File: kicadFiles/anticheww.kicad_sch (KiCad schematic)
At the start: 423 parts, among them J1 TYPE-C-31-M12_13, J2 ARM JTAG, Q1 AO3401A, Q2 DTC123JKAT146, Q3 DTC123JKAT146, SW1 ESC, SW10 9, SW11 0, SW12 MINUS, SW13 PLUS, SW14 LBKSP, SW15 RBKSP, SW16 Rotary_Encoder_Switch_Chassis, SW17 2U_BKSP, SW18 Rotary_Encoder_Switch_Chassis, SW19 TAB, SW2 1, SW20 Q, SW21 W, SW22 E, SW23 R, SW24 T, SW25 Y, SW26 U, SW27 I, SW28 O, SW29 P, SW3 2, SW30 LBRKT, SW31 RBRKT, SW32 BKSLSH, SW33 PGDN, SW34 ISO_ENTER, SW35 Rotary_Encoder_Switch_Chassis, SW36 CAPS, SW37 A, SW38 S, SW39 D, SW4 3, SW40 F, SW41 G, SW42 H, SW43 J, SW44 K, SW45 L, SW46 COLON, SW47 QUOTE, SW48 ENTER, SW49 HOME, SW5 4, SW50 PGUP, SW51 STEPPED_CAPS, SW52 ISO_TILDE, SW53 Rotary_Encoder_Switch_Chassis, SW54 LSHFT, SW55 ISO_BKLSH, SW56 Z, SW57 X, SW58 C, SW59 V, SW6 5, SW60 B, SW61 N, SW62 M, SW63 COMMA, SW64 DOT, SW65 SLSH, SW66 175_RSHFT, SW67 UP, SW68 END, SW69 ISO_LSHFT, SW7 6, SW70 275_RSHFT, SW71 LCTRL, SW72 LGUI, SW73 LALT, SW74 SPC, SW75 RALT, SW76 RGUI, SW77 RCTRL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

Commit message: Finish routing, DRC pending
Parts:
- removed R26: 10k, Resistor_SMD:R_0805_2012Metric, symbol Device:R
- added D89, D90, D91, D92: 1N4148W, acheron_Components:D_SOD-123, symbol Device:D
- renumbered SW16 to ROT1, SW18 to ROT2, SW35 to ROT3, SW53 to ROT4
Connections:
- net ENCB: now also ROT1.B, ROT2.B, ROT3.B, ROT4.B
- net GND: now also ROT1.S (Shield), ROT2.S (Shield), ROT3.S (Shield), ROT4.S (Shield)
- net RGB_3V3: now also U3.28 (SPI2_MOSI/I2S2_SD/PB15)
- net ROTB: now also U3.18 (PB0/TIM3_CH3/ADC_IN8)
- net R0: now reaches D1.1 (K), D10.1 (K), D11.1 (K), D12.1 (K), D13.1 (K), D14.1 (K), D15.1 (K), D2.1 (K), D3.1 (K), D4.1 (K), D5.1 (K), D6.1 (K), D7.1 (K), D8.1 (K), D9.1 (K)
- net R0: now also U3.30 (TIM1_CH2/PA9)
- net ENCA: now reaches ROT2.A
- net ENCA: now also R94.2, R96.1, ROT1.A, ROT3.A, ROT4.A
- net at ROT2.C: now also D90.2 (A)
- net C14: now reaches ROT2.S1
- net C14: now also ROT1.S1, ROT4.S1, SW15.1 (Col), SW17.1 (Col), SW33.1 (Col), SW50.1 (Col), SW68.1 (Col), SW80.1 (Col), U3.39 (SPI1_SCK/I2S1_CK/TIM2_CH2/PB3)
- net R2_S2: now reaches ROT2.S2
- net R2_S2: now also D30.2 (A), SW33.2 (Row)
- net C1: now reaches SW2.1 (Col), SW20.1 (Col), SW37.1 (Col), SW55.1 (Col), SW72.1 (Col), SW82.1 (Col)
- net C1: now also U3.11 (PA1/ADC_IN1)
- net R1: now reaches D16.1 (K), D17.1 (K), D18.1 (K), D19.1 (K), D20.1 (K), D21.1 (K), D22.1 (K), D23.1 (K), D24.1 (K), D25.1 (K), D26.1 (K), D27.1 (K), D28.1 (K), D29.1 (K)
- net R1: now also D45.1 (K), U3.38 (PA15), D89.1 (K); no longer D30.1 (K)
- net C13: now reaches SW14.1 (Col), SW32.1 (Col), SW34.1 (Col), SW49.1 (Col), SW67.1 (Col), SW79.1 (Col)
- net C13: now also ROT3.S1, U3.40 (SPI1_MISO/I2S1_MCK/TIM3_CH1/PB4)
- net R5: now reaches D32.1 (K), D33.1 (K), D34.1 (K), D35.1 (K), D36.1 (K), D37.1 (K), D38.1 (K), D39.1 (K), D40.1 (K), D41.1 (K), D42.1 (K), D43.1 (K), D44.1 (K)
- net R5: now also D30.1 (K), D90.1 (K); no longer D31.1 (K), D45.1 (K)
- net C12: now reaches SW13.1 (Col), SW31.1 (Col), SW48.1 (Col), SW52.1 (Col), SW66.1 (Col), SW70.1 (Col), SW78.1 (Col)
- net C12: now also U3.41 (SPI1_MOSI/I2S1_SD/TIM3_CH2/PB5)
- net C2: now reaches SW21.1 (Col), SW3.1 (Col), SW38.1 (Col), SW56.1 (Col), SW73.1 (Col), SW83.1 (Col)
- net C2: now also U3.10 (PA0/ADC_IN0)
- net C8: now reaches SW27.1 (Col), SW44.1 (Col), SW62.1 (Col), SW87.1 (Col), SW9.1 (Col), SW90.1 (Col)
- net C8: now also U3.46 (SPI2_NSS/I2S2_WS/I2C1_SDA/TIM17_CH1/PB9)
- net C5: now reaches SW24.1 (Col), SW41.1 (Col), SW59.1 (Col), SW6.1 (Col)
- net C5: now also U3.4 (PC15/OSC32_OUT)
- net C11: now reaches SW12.1 (Col), SW30.1 (Col), SW47.1 (Col), SW65.1 (Col), SW77.1 (Col)
- net C11: now also U3.42 (I2C1_SCL/PB6)
- net C6: now reaches SW25.1 (Col), SW42.1 (Col), SW60.1 (Col), SW7.1 (Col), SW74.1 (Col), SW84.2 (Row), SW86.1 (Col), SW89.1 (Col)
- net C6: now also U3.3 (PC14/OSC32_IN)
- net C7: now reaches SW26.1 (Col), SW43.1 (Col), SW61.1 (Col), SW8.1 (Col)
- net C7: now also U3.2 (PC13)
- net ROTA: now reaches C17.1, R96.2
- net ROTA: now also U3.17 (PA7/TIM3_CH2/TIM14_CH1/ADC_IN7)
- net C10: now reaches SW11.1 (Col), SW29.1 (Col), SW46.1 (Col), SW64.1 (Col), SW76.1 (Col)
- net C10: now also U3.43 (2C1_SDA/PB7)
- net R4: now reaches D61.1 (K), D62.1 (K), D63.1 (K), D64.1 (K), D65.1 (K), D66.1 (K), D67.1 (K), D68.1 (K), D69.1 (K), D70.1 (K), D71.1 (K), D72.1 (K)
- net R4: now also U3.29 (TIM1_CH1/PA8), D92.1 (K)
- net C0: now reaches SW1.1 (Col), SW19.1 (Col), SW36.1 (Col), SW51.1 (Col), SW54.1 (Col), SW69.1 (Col), SW71.1 (Col), SW81.1 (Col)
- net R3_S2: now reaches D44.2 (A), SW49.2 (Row)
- net R3_S2: now also ROT3.S2
- net R3: now reaches D46.1 (K), D47.1 (K), D48.1 (K), D49.1 (K), D50.1 (K), D51.1 (K), D52.1 (K), D53.1 (K), D54.1 (K), D55.1 (K), D56.1 (K), D57.1 (K), D58.1 (K), D59.1 (K), D60.1 (K)
- net R3: now also U3.27 (SPI2_MISO/I2S2_MCK/I2C2_SDA/TIM15_CH1/PB14), D91.1 (K)
- net C4: now reaches SW23.1 (Col), SW40.1 (Col), SW5.1 (Col), SW58.1 (Col), SW85.1 (Col), SW88.1 (Col)
- net C4: now also U3.5 (PF0/OSC_IN)
- net R2: now reaches U3.31 (TIM1_CH3/PA10)
- net R2: now also D31.1 (K)
- net C9: now reaches U3.45 (I2C1_SCL/TIM16_CH1/PB8)
- net C9: now also SW10.1 (Col), SW28.1 (Col), SW45.1 (Col), SW63.1 (Col), SW75.1 (Col)
- net C3: now reaches U3.6 (PF1/OSC_OUT)
- net C3: now also SW22.1 (Col), SW39.1 (Col), SW4.1 (Col), SW57.1 (Col)
- net at ROT3.C: now also D91.2 (A)
- net R4_S2: now reaches D60.2 (A), SW68.2 (Row)
- net R4_S2: now also ROT4.S2
- net R1_S2: now reaches D45.2 (A), SW50.2 (Row)
- net R1_S2: now also ROT1.S2
- net at ROT4.C: now also D92.2 (A)
- net at ROT1.C: now also D89.2 (A)
- no-connect marks 1 -> 2
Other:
- moved on the sheet: D30, D45, SW33, SW50

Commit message: Organize schematic and reset annotations
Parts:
- added SW87: RALT_125, acheron_MX_SolderMask:MX125, symbol acheronSymbols:MXSwitch
- added SW88: RGUI_125, acheron_MX_SolderMask:MX125, symbol acheronSymbols:MXSwitch
- added SW89: RGUI_150, acheron_MX_SolderMask:MX150, symbol acheronSymbols:MXSwitch
- U2: renamed from U3; value STM32F072-LQFP48 -> STM32F072CBT6
- renumbered C17 to C1, C8 to C10, C9 to C11, C10 to C12, C11 to C13, C12 to C14, C13 to C15, C14 to C16, C15 to C17, C16 to C18, C18 to C2, C26 to C23, C27 to C24, C29 to C25, C30 to C26, C23 to C27, C24 to C28, C25 to C29, C1 to C3, C28 to C30, C2 to C4, C3 to C5, C4 to C6, C5 to C7, C6 to C8, C7 to C9, D89 to D1, D78 to D10, D79 to D11, D80 to D12, D81 to D13, D82 to D14, D83 to D15, D84 to D16, D85 to D17, D86 to D18, D1 to D19, D90 to D2, D2 to D20, D3 to D21, D4 to D22, D5 to D23, D6 to D24, D7 to D25, D8 to D26, D9 to D27, D10 to D28, D11 to D29, D91 to D3, D12 to D30, D13 to D31, D14 to D32, D15 to D33, D16 to D34, D17 to D35, D18 to D36, D19 to D37, D20 to D38, D21 to D39, D92 to D4, D22 to D40, D23 to D41, D24 to D42, D25 to D43, D26 to D44, D27 to D45, D28 to D46, D29 to D47, D45 to D48, D31 to D49, D73 to D5, D32 to D50, D33 to D51, D34 to D52, D35 to D53, D36 to D54, D37 to D55, D38 to D56, D39 to D57, D40 to D58, D41 to D59, D74 to D6, D42 to D60, D43 to D61, D44 to D62, D30 to D63, D46 to D64, D47 to D65, D48 to D66, D49 to D67, D50 to D68, D51 to D69, D75 to D7, D52 to D70, D53 to D71, D54 to D72, D55 to D73, D56 to D74, D57 to D75, D58 to D76, D59 to D77, D60 to D78, D61 to D79, D76 to D8, D62 to D80, D63 to D81, D64 to D82, D65 to D83, D66 to D84, D67 to D85, D68 to D86, D69 to D87, D70 to D88, D71 to D89, D77 to D9, D72 to D90, D87 to D91, D88 to D92, J2 to J1, J1 to J2, R94 to R1, R8 to R10, R101 to R100, R102 to R101, R9 to R11, R27 to R12, R28 to R13, R29 to R14, R30 to R15, R31 to R16, R32 to R17, R33 to R18, R1 to R19, R95 to R2, R2 to R20, R10 to R21, R11 to R22, R12 to R23, R13 to R24, R14 to R25, R15 to R26, R16 to R27, R17 to R28, R18 to R29, R96 to R3, R19 to R30, R20 to R31, R21 to R32, R22 to R33, R23 to R34, R24 to R35, R25 to R36, R34 to R37, R35 to R38, R36 to R39, R97 to R4, R37 to R40, R38 to R41, R39 to R42, R40 to R43, R41 to R44, R42 to R45, R43 to R46, R44 to R47, R45 to R48, R46 to R49, R3 to R5, R47 to R50, R48 to R51, R49 to R52, R50 to R53, R51 to R54, R52 to R55, R53 to R56, R54 to R57, R55 to R58, R56 to R59, R4 to R6, R57 to R60, R58 to R61, R59 to R62, R60 to R63, R61 to R64, R62 to R65, R63 to R66, R64 to R67, R65 to R68, R66 to R69, R5 to R7, R67 to R70, R68 to R71, R69 to R72, R70 to R73, R71 to R74, R72 to R75, R73 to R76, R74 to R77, R75 to R78, R76 to R79, R6 to R8, R77 to R80, R78 to R81, R79 to R82, R80 to R83, R81 to R84, R82 to R85, R83 to R86, R84 to R87, R85 to R88, R86 to R89, R7 to R9, R87 to R90, R88 to R91, R89 to R92, R90 to R93, R91 to R94, R92 to R95, R93 to R96, R98 to R97, R99 to R98, R100 to R99, SW17 to SW16, SW19 to SW17, SW20 to SW18, SW21 to SW19, SW22 to SW20, SW23 to SW21, SW24 to SW22, SW25 to SW23, SW26 to SW24, SW27 to SW25, SW28 to SW26, SW29 to SW27, SW30 to SW28, SW31 to SW29, SW32 to SW30, SW50 to SW31, SW34 to SW32, SW36 to SW33, SW37 to SW34, SW38 to SW35, SW39 to SW36, SW40 to SW37, SW41 to SW38, SW42 to SW39, SW43 to SW40, SW44 to SW41, SW45 to SW42, SW46 to SW43, SW47 to SW44, SW48 to SW45, SW49 to SW46, SW33 to SW47, SW51 to SW48, SW52 to SW49, SW54 to SW50, SW55 to SW51, SW56 to SW52, SW57 to SW53, SW58 to SW54, SW59 to SW55, SW60 to SW56, SW61 to SW57, SW62 to SW58, SW63 to SW59, SW64 to SW60, SW65 to SW61, SW66 to SW62, SW67 to SW63, SW68 to SW64, SW69 to SW65, SW70 to SW66, SW71 to SW67, SW72 to SW68, SW73 to SW69, SW74 to SW70, SW75 to SW71, SW76 to SW72, SW77 to SW73, SW78 to SW74, SW79 to SW75, SW80 to SW76, SW81 to SW77, SW82 to SW78, SW83 to SW79, SW84 to SW80, SW85 to SW81, SW86 to SW82, SW87 to SW83, SW88 to SW84, SW89 to SW85, SW90 to SW86, U2 to U3
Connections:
- net C10: now also SW88.1 (Col), SW89.1 (Col)
- net C9: now also SW87.1 (Col)
- net S8: now reaches D84.2 (A), SW72.2 (Row)
- net S8: now also SW88.2 (Row), SW89.2 (Row)
- net S7: now reaches D83.2 (A), SW71.2 (Row)
- net S7: now also SW87.2 (Row)
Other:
- note added: "225-125-275 (S1)"
- note added: "275-125-225 (S2)"
- note added: "6.25U (D)"
- note added: "7U (T)"
- note added: "ENCODERS"
- note added: "GRAPHICS"
- note added: "LED"
- note added: "RGB BACKLIGHT"
- note added: "SWITCH MATRIX"
- note added: "USB"
- moved on the sheet: C1, C10, C11, C12, C13, C14, C15, C16, C17, C18, C19, C2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

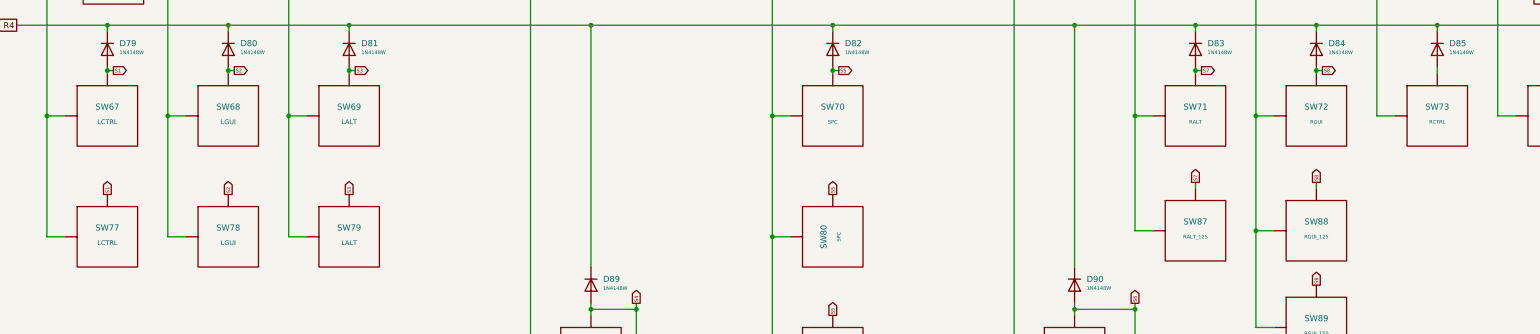
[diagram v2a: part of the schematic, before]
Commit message: Add 0.5 blocker layout options
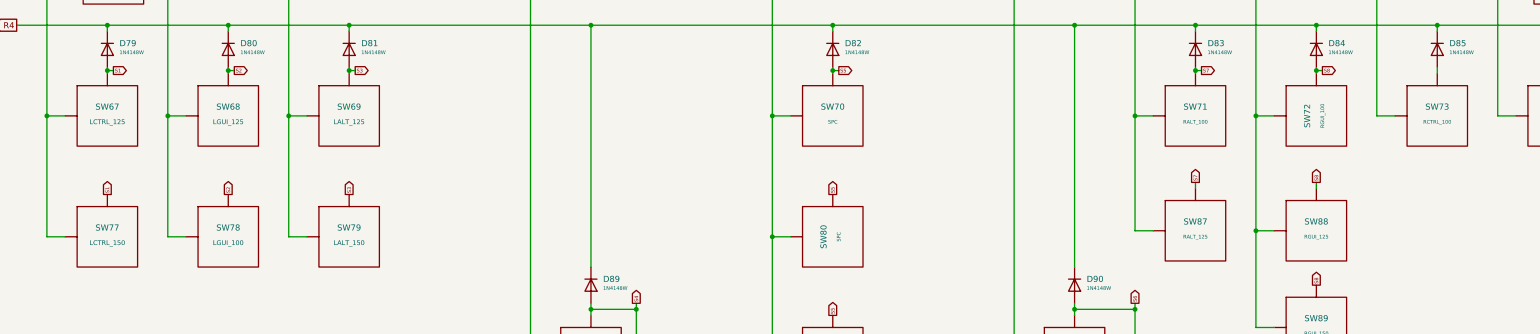
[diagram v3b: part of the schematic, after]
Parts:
- SW67: value LCTRL -> LCTRL_125
- SW68: value LGUI -> LGUI_125
- SW69: value LALT -> LALT_125
- SW71: value RALT -> RALT_100
- SW72: value RGUI -> RGUI_100
- SW73: value RCTRL -> RCTRL_100
- SW77: value LCTRL -> LCTRL_150
- SW78: value LGUI -> LGUI_100
- SW79: value LALT -> LALT_150
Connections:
- net C10: now also SW72.2 (Row); no longer SW72.1 (Col)
- net S8: now also SW72.1 (Col); no longer SW72.2 (Row)
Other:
- moved on the sheet: SW72
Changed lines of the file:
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@@
     (title "Anticheww")
     (date "2020-07-31")
-    (rev "V2.0.5")
+    (rev "V2.0.6")
     (company "Designed by Gondolindrim")
     (comment 1 "In partnership with Chewwy")
@@
   (junction (at 783.59 285.75) (diameter 1.016) (color 0 0 0 0))
   (junction (at 783.59 298.45) (diameter 1.016) (color 0 0 0 0))
-  (no_connect (at 724.916 494.665))
   (no_connect (at 785.876 419.1))
+  (no_connect (at 724.916 494.665))
   (wire (pts (xy 57.15 50.8) (xy 76.2 50.8))
     (stroke (width 0) (type solid) (color 0 0 0 0))
@@
     (in_bom no) (on_board yes)
     (property "Reference" "SW67" (id 0) (at 76.2 194.945 0))
-    (property "Value" "LCTRL" (id 1) (at 76.2 198.12 0)
+    (property "Value" "LCTRL_125" (id 1) (at 76.2 198.12 0)
       (effects (font (size 0.9906 0.9906)))
     )
@@
     (in_bom no) (on_board yes)
     (property "Reference" "SW77" (id 0) (at 76.2 220.345 0))
-    (property "Value" "LCTRL" (id 1) (at 76.2 223.52 0)
+    (property "Value" "LCTRL_150" (id 1) (at 76.2 223.52 0)
       (effects (font (size 0.9906 0.9906)))
     )
@@
     (in_bom no) (on_board yes)
     (property "Reference" "SW68" (id 0) (at 101.6 194.945 0))
-    (property "Value" "LGUI" (id 1) (at 101.6 198.12 0)
+    (property "Value" "LGUI_125" (id 1) (at 101.6 198.12 0)
       (effects (font (size 0.9906 0.9906)))
     )
@@
     (in_bom no) (on_board yes)
     (property "Reference" "SW78" (id 0) (at 101.6 220.345 0))
-    (property "Value" "LGUI" (id 1) (at 101.6 223.52 0)
+    (property "Value" "LGUI_100" (id 1) (at 101.6 223.52 0)
       (effects (font (size 0.9906 0.9906)))
     )
@@
     (in_bom no) (on_board yes)
     (property "Reference" "SW69" (id 0) (at 127 194.945 0))
-    (property "Value" "LALT" (id 1) (at 127 198.12 0)
+    (property "Value" "LALT_125" (id 1) (at 127 198.12 0)
       (effects (font (size 0.9906 0.9906)))
     )
@@
     (in_bom no) (on_board yes)
     (property "Reference" "SW79" (id 0) (at 127 220.345 0))
-    (property "Value" "LALT" (id 1) (at 127 223.52 0)
+    (property "Value" "LALT_150" (id 1) (at 127 223.52 0)
       (effects (font (size 0.9906 0.9906)))
     )
@@
     (in_bom no) (on_board yes)
     (property "Reference" "SW71" (id 0) (at 304.8 194.945 0))
-    (property "Value" "RALT" (id 1) (at 304.8 198.12 0)
+    (property "Value" "RALT_100" (id 1) (at 304.8 198.12 0)
       (effects (font (size 0.762 0.762)))
     )
@@
     )
   )
-  (symbol (lib_id "acheronSymbols:MXSwitch") (at 330.2 196.85 0) (unit 1)
+  (symbol (lib_id "acheronSymbols:MXSwitch") (at 330.2 196.85 90) (mirror x) (unit 1)
     (in_bom no) (on_board yes)
-    (property "Reference" "SW72" (id 0) (at 330.2 194.945 0))
-    (property "Value" "RGUI" (id 1) (at 330.2 198.12 0)
+    (property "Reference" "SW72" (id 0) (at 328.295 196.85 0))
+    (property "Value" "RGUI_100" (id 1) (at 331.47 196.85 0)
       (effects (font (size 0.762 0.762)))
     )
@@
     (in_bom no) (on_board yes)
     (property "Reference" "SW73" (id 0) (at 355.6 194.945 0))
-    (property "Value" "RCTRL" (id 1) (at 355.6 198.12 0)
+    (property "Value" "RCTRL_100" (id 1) (at 355.6 198.12 0)
       (effects (font (size 0.762 0.762)))
     )

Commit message: Added ANTICHEWW plated logo
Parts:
- added GR6: Anticheww Plated Logo, antichewwGraphics:antichewwLogo_67.9x5, symbol Mechanical:MountingHole
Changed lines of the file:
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@@
   (title_block
     (title "Anticheww")
-    (date "2020-07-31")
-    (rev "V2.0.6")
+    (date "2020-08-01")
+    (rev "V2.0.7")
     (company "Designed by Gondolindrim")
     (comment 1 "In partnership with Chewwy")
@@
     )
   )
+  (symbol (lib_id "Mechanical:MountingHole") (at 616.585 250.825 0) (unit 1)
+    (in_bom no) (on_board yes)
+    (property "Reference" "GR6" (id 0) (at 619.1251 249.6756 0)
+      (effects (font (size 1.27 1.27)) (justify left))
+    )
+    (property "Value" "Anticheww Plated Logo" (id 1) (at 619.1251 251.9743 0)
+      (effects (font (size 1.27 1.27)) (justify left))
+    )
+    (property "Footprint" "antichewwGraphics:antichewwLogo_67.9x5" (id 2) (at 616.585 250.825 0)
+      (effects (font (size 1.27 1.27)) hide)
+    )
+    (property "Datasheet" "~" (id 3) (at 616.585 250.825 0)
+      (effects (font (size 1.27 1.27)) hide)
+    )
+  )
   (symbol (lib_id "Mechanical:MountingHole") (at 622.3 311.15 0) (unit 1)
     (in_bom no) (on_board yes)
@@
       (reference "GR5") (unit 1)
     )
+    (path "/d9f1ff38-2184-4184-a7be-c474c16ae384"
+      (reference "GR6") (unit 1)
+    )
     (path "/00000000-0000-0000-0000-00005d878ca4"

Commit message: Fixed bottom row silkscreen markings and added ISO/ANSI enter markings
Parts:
- added LED87, LED? (x2): LED, acheron_Components:LED_THT_2.54mm, symbol acheronSymbols:LED
- SW70: value SPC -> SPC_625
- SW80: value SPC -> SPC_700
- SW82: value 125_SPC -> SPC_125
- SW85: value SPC -> SPC_125
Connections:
- net GND: now also LED87.K, LED?.K, LED?.K
- net at LED81.A, R89.1: now also LED?.A, LED?.A
- net at LED80.A, R88.1: now also LED87.A
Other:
- moved on the sheet: LED81, LED82, LED83, LED84, LED85, LED86, R89, R90, R91, R92, R93, R94

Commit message: Add labels, organized F.Fab
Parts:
- added GR7: Anticheww Plated Label, antichewwGraphics:antichewwLabel_75x2mm, symbol Mechanical:MountingHole
- added GR8: Anticheww Plated Label, antichewwGraphics:antichewwLabel_60.9x1.9mm, symbol Mechanical:MountingHole
- added J3: Conn_02x05_Odd_Even, Connector_PinHeader_1.00mm:PinHeader_2x05_P1.00mm_Vertical, symbol Connector_Generic:Conn_02x05_Odd_Even
- J2: value TYPE-C-31-M12_13 -> TYPE-C-31-M-12
- gave numbers to parts that had none: 2
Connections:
- net 3V3: now also J3.1 (Pin_1)
- net GND: now also J3.2 (Pin_2)
- net R5: now also U2.12 (PA2/ADC_IN2)
- net EXTRA10: now reaches U2.13 (PA3/TIM15_CH2/ADC_IN3)
- net EXTRA10: now also J3.10 (Pin_10)
- net EXTRA8: now reaches U2.14 (PA4/TIM14_CH1/ADC_IN4)
- net EXTRA8: now also J3.8 (Pin_8)
- net EXTRA6: now reaches U2.15 (PA5/ADC_IN5/DAC_OUT2)
- net EXTRA6: now also J3.6 (Pin_6)
- net EXTRA9: now reaches U2.19 (PB1/TIM3_CH4/TIM14_CH1/ADC_IN9)
- net EXTRA9: now also J3.9 (Pin_9)
- net EXTRA7: now reaches U2.20 (PB2)
- net EXTRA7: now also J3.7 (Pin_7)
- net EXTRA5: now reaches U2.21 (PB10/SPI2_SCK/I2C2_SCL/TIM2_CH3)
- net EXTRA5: now also J3.5 (Pin_5)
- net EXTRA3: now reaches U2.22 (PB11/TIM2_CH4/I2C2_SDA)
- net EXTRA3: now also J3.3 (Pin_3)
- net EXTRA4: now reaches U2.25 (PB12)
- net EXTRA4: now also J3.4 (Pin_4)
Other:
- note added: "6.25 blocker (DB)"
- note added: "625 (SD)"
- note added: "7.00 blocker (TB)"
- note added: "700 (T)"
- note added: "No blocker (N)"
- moved on the sheet: C19, C20, C21, C22, C23, C24, C25, C26, D90, GR1, GR2, GR3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
